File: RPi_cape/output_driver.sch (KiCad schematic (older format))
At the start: 20 parts, among them Q1 NTD5865NLT4G, U8 74LVC1G08, U9 EL3H7(TA)-VG

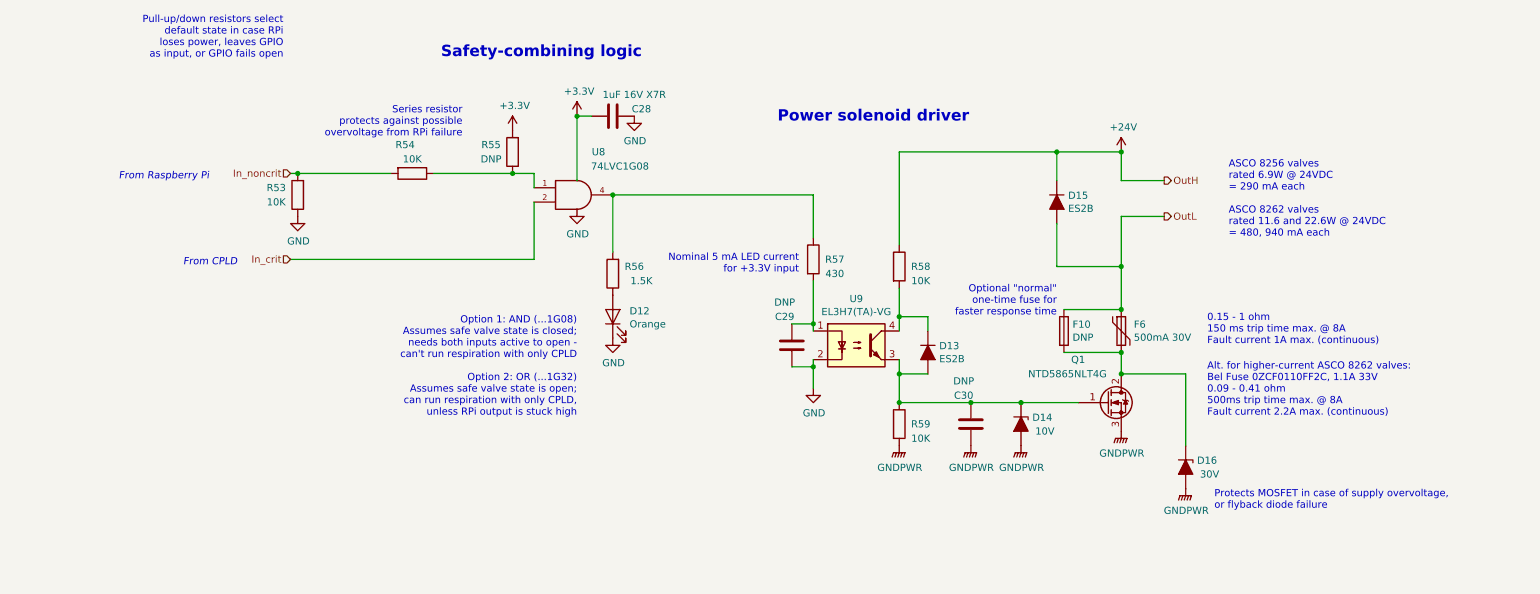
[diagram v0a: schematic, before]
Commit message: Extra info, post-design-review fixes
Added extra info on existing alternate circuit options
Added extra info on parts selection
Created initial PCB file
Added bulk cap to +5V input
Design review fixes:
Moved Raspberry Pi PWM output to GPIO18 to take advantage of hardware PWM
Fixed floating shutdown input on audio amp
Added series resistor R177 to allow low battery output to signal to both CPLD and external LED at the same time
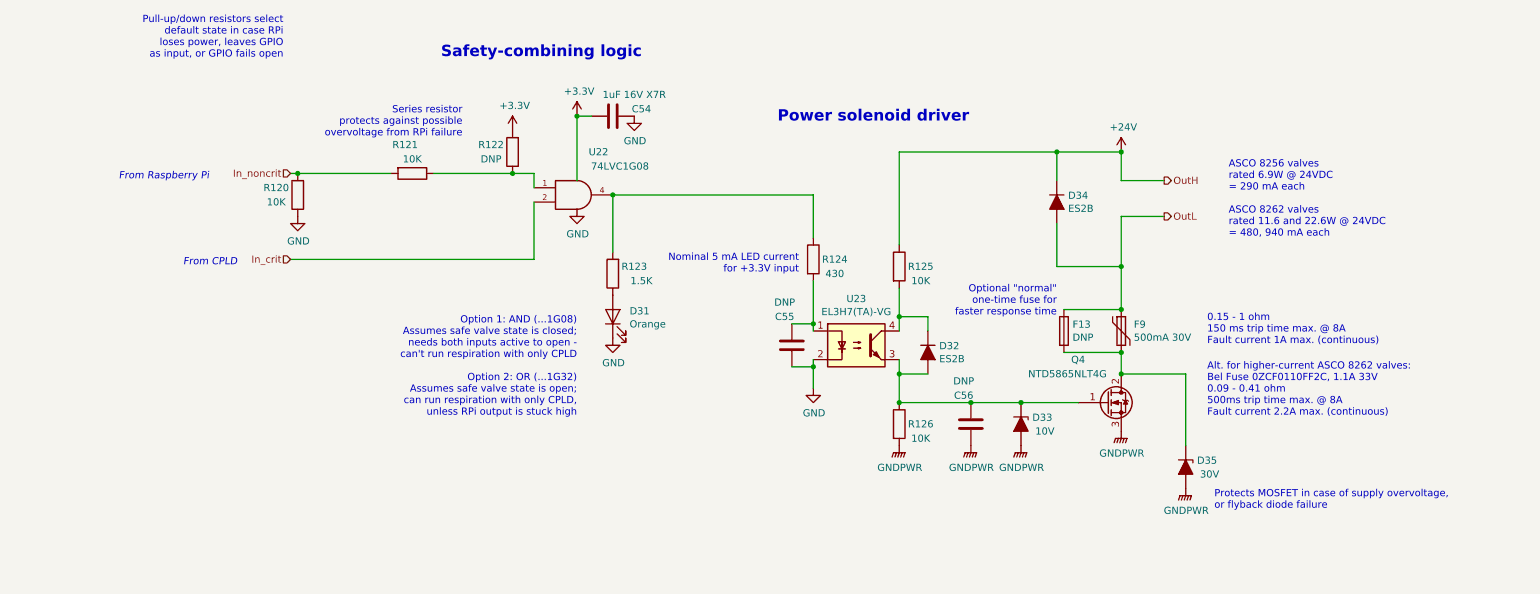
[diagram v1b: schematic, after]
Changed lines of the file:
@@
 AR Path="/5E8DFCAD/5E8FC2C2" Ref="U21"  Part="1"
 AR Path="/5E8E0754/5E8FC2C2" Ref="U23"  Part="1"
-F 0 "U9" H 6450 4025 50  0000 C CNN
+F 0 "U23" H 6450 4025 50  0000 C CNN
 F 1 "EL3H7(TA)-VG" H 6450 3934 50  0000 C CNN
 F 2 "Package_SO:SOIC-4_4.55x2.6mm_P1.27mm" H 6250 3500 50  0001 L CIN
@@
 AR Path="/5E8DFCAD/5E8FF47A" Ref="R117"  Part="1"
 AR Path="/5E8E0754/5E8FF47A" Ref="R124"  Part="1"
-F 0 "R57" H 6300 3100 50  0000 C CNN
+F 0 "R124" H 6300 3100 50  0000 C CNN
 F 1 "430" H 6300 3000 50  0000 C CNN
 F 2 "Resistor_SMD:R_1206_3216Metric" V 6080 3100 50  0001 C CNN
@@
 AR Path="/5E8DFCAD/5E900D57" Ref="#PWR0183"  Part="1"
 AR Path="/5E8E0754/5E900D57" Ref="#PWR0196"  Part="1"
-F 0 "#PWR0106" H 6150 3750 50  0001 C CNN
+F 0 "#PWR0196" H 6150 3750 50  0001 C CNN
 F 1 "GND" H 6155 3827 50  0000 C CNN
 F 2 "" H 6150 4000 50  0001 C CNN
@@
 AR Path="/5E8DFCAD/5E901311" Ref="R118"  Part="1"
 AR Path="/5E8E0754/5E901311" Ref="R125"  Part="1"
-F 0 "R58" H 6900 3150 50  0000 C CNN
+F 0 "R125" H 6900 3150 50  0000 C CNN
 F 1 "10K" H 6900 3050 50  0000 C CNN
 F 2 "Resistor_SMD:R_1206_3216Metric" V 6680 3150 50  0001 C CNN
@@
 AR Path="/5E8DFCAD/5E9015BE" Ref="R119"  Part="1"
 AR Path="/5E8E0754/5E9015BE" Ref="R126"  Part="1"
-F 0 "R59" H 6900 4250 50  0000 C CNN
+F 0 "R126" H 6900 4250 50  0000 C CNN
 F 1 "10K" H 6900 4150 50  0000 C CNN
 F 2 "Resistor_SMD:R_1206_3216Metric" V 6680 4250 50  0001 C CNN
@@
 AR Path="/5E8DFCAD/5E905A02" Ref="C53"  Part="1"
 AR Path="/5E8E0754/5E905A02" Ref="C56"  Part="1"
-F 0 "C30" H 7200 4050 50  0000 C CNN
+F 0 "C56" H 7200 4050 50  0000 C CNN
 F 1 "DNP" H 7200 3950 50  0000 C CNN
 F 2 "Capacitor_SMD:C_0805_2012Metric" H 7288 4100 50  0001 C CNN
@@
 AR Path="/5E8DFCAD/5E9088A7" Ref="D28"  Part="1"
 AR Path="/5E8E0754/5E9088A7" Ref="D33"  Part="1"
-F 0 "D14" V 7554 4329 50  0000 L CNN
+F 0 "D33" V 7554 4329 50  0000 L CNN
 F 1 "10V" V 7650 4350 50  0000 L CNN
 F 2 "Diode_SMD:D_SOD-123" H 7600 4250 50  0001 C CNN
@@
 AR Path="/5E8DFCAD/5E908F8A" Ref="Q3"  Part="1"
 AR Path="/5E8E0754/5E908F8A" Ref="Q4"  Part="1"
-F 0 "Q1" H 7950 4400 50  0000 L CNN
+F 0 "Q4" H 7950 4400 50  0000 L CNN
 F 1 "NTD5865NLT4G" H 7650 4300 50  0000 L CNN
 F 2 "Package_TO_SOT_SMD:TO-252-2" H 8400 4200 50  0001 C CNN
@@
 AR Path="/5E8DFCAD/5E909869" Ref="F8"  Part="1"
 AR Path="/5E8E0754/5E909869" Ref="F9"  Part="1"
-F 0 "F6" H 8388 3646 50  0000 L CNN
+F 0 "F9" H 8388 3646 50  0000 L CNN
 F 1 "500mA 30V" H 8388 3555 50  0000 L CNN
 F 2 "Fuse:Fuse_2920_7451Metric" H 8350 3400 50  0001 L CNN
@@
 AR Path="/5E8DFCAD/5E90C94B" Ref="D30"  Part="1"
 AR Path="/5E8E0754/5E90C94B" Ref="D35"  Part="1"
-F 0 "D16" V 8704 4629 50  0000 L CNN
+F 0 "D35" V 8704 4629 50  0000 L CNN
 F 1 "30V" V 8800 4650 50  0000 L CNN
 F 2 "Diode_SMD:D_SMA" H 8750 4550 50  0001 C CNN
@@
 AR Path="/5E8DFCAD/5E90D582" Ref="D29"  Part="1"
 AR Path="/5E8E0754/5E90D582" Ref="D34"  Part="1"
-F 0 "D15" V 7804 2779 50  0000 L CNN
+F 0 "D34" V 7804 2779 50  0000 L CNN
 F 1 "ES2B" V 7895 2779 50  0000 L CNN
 F 2 "Diode_SMD:D_SMA" H 7850 2700 50  0001 C CNN
@@
 AR Path="/5E8DFCAD/5E913275" Ref="D27"  Part="1"
 AR Path="/5E8E0754/5E913275" Ref="D32"  Part="1"
-F 0 "D13" V 6904 3829 50  0000 L CNN
+F 0 "D32" V 6904 3829 50  0000 L CNN
 F 1 "ES2B" V 6995 3829 50  0000 L CNN
 F 2 "Diode_SMD:D_SMA" H 6950 3750 50  0001 C CNN
@@
 AR Path="/5E8DFCAD/5E880DD0" Ref="#PWR0189"  Part="1"
 AR Path="/5E8E0754/5E880DD0" Ref="#PWR0202"  Part="1"
-F 0 "#PWR0112" H 8750 4500 50  0001 C CNN
+F 0 "#PWR0202" H 8750 4500 50  0001 C CNN
 F 1 "GNDPWR" H 8754 4546 50  0000 C CNN
 F 2 "" H 8750 4650 50  0001 C CNN
@@
 AR Path="/5E8DFCAD/5E8842DE" Ref="#PWR0187"  Part="1"
 AR Path="/5E8E0754/5E8842DE" Ref="#PWR0200"  Part="1"
-F 0 "#PWR0110" H 8300 2200 50  0001 C CNN
+F 0 "#PWR0200" H 8300 2200 50  0001 C CNN
 F 1 "+24V" H 8315 2523 50  0000 C CNN
 F 2 "" H 8300 2350 50  0001 C CNN
@@
 AR Path="/5E8DFCAD/5E88C1E4" Ref="C52"  Part="1"
 AR Path="/5E8E0754/5E88C1E4" Ref="C55"  Part="1"
-F 0 "C29" H 5950 3500 50  0000 C CNN
+F 0 "C55" H 5950 3500 50  0000 C CNN
 F 1 "DNP" H 5950 3400 50  0000 C CNN
 F 2 "Capacitor_SMD:C_0805_2012Metric" H 6038 3550 50  0001 C CNN
@@
 AR Path="/5E8DFCAD/5EA15643" Ref="U20"  Part="1"
 AR Path="/5E8DEDC0/5EA15643" Ref="U18"  Part="1"
-F 0 "U8" H 4650 2950 50  0000 C CNN
+F 0 "U22" H 4650 2950 50  0000 C CNN
 F 1 "74LVC1G08" H 4800 2850 50  0000 C CNN
 F 2 "Package_TO_SOT_SMD:SOT-23-5" H 4500 2650 50  0001 C CNN
@@
 AR Path="/5E8DFCAD/5EA17709" Ref="#PWR0180"  Part="1"
 AR Path="/5E8E0754/5EA17709" Ref="#PWR0193"  Part="1"
-F 0 "#PWR0103" H 4500 2500 50  0001 C CNN
+F 0 "#PWR0193" H 4500 2500 50  0001 C CNN
 F 1 "GND" H 4505 2577 50  0000 C CNN
 F 2 "" H 4500 2750 50  0001 C CNN
@@
 AR Path="/5E8DFCAD/5EA197B0" Ref="#PWR0179"  Part="1"
 AR Path="/5E8DEDC0/5EA197B0" Ref="#PWR0166"  Part="1"
-F 0 "#PWR0102" H 4500 1950 50  0001 C CNN
+F 0 "#PWR0192" H 4500 1950 50  0001 C CNN
 F 1 "+3.3V" H 4515 2273 50  0000 C CNN
 F 2 "" H 4500 2100 50  0001 C CNN
@@
 AR Path="/5E8DFCAD/5EA25A46" Ref="#PWR0182"  Part="1"
 AR Path="/5E8DEDC0/5EA25A46" Ref="#PWR0169"  Part="1"
-F 0 "#PWR0105" H 4900 1850 50  0001 C CNN
+F 0 "#PWR0195" H 4900 1850 50  0001 C CNN
 F 1 "GND" H 4905 1927 50  0000 C CNN
 F 2 "" H 4900 2100 50  0001 C CNN
@@
 AR Path="/5E8DFCAD/5EA25A4C" Ref="C51"  Part="1"
 AR Path="/5E8DEDC0/5EA25A4C" Ref="C48"  Part="1"
-F 0 "C28" V 4700 2300 50  0000 C CNN
+F 0 "C54" V 4700 2300 50  0000 C CNN
 F 1 "1uF 16V X7R" V 4600 2250 50  0000 C CNN
 F 2 "Capacitor_SMD:C_0805_2012Metric" H 4788 1950 50  0001 C CNN
@@
 AR Path="/5E8DFCAD/5EAB3FCE" Ref="R113"  Part="1"
 AR Path="/5E8E0754/5EAB3FCE" Ref="R120"  Part="1"
-F 0 "R53" H 2700 2600 50  0000 C CNN
+F 0 "R120" H 2700 2600 50  0000 C CNN
 F 1 "10K" H 2700 2700 50  0000 C CNN
 F 2 "Resistor_SMD:R_1206_3216Metric" V 2480 2650 50  0001 C CNN
@@
 AR Path="/5E8DFCAD/5EAB68F6" Ref="#PWR0177"  Part="1"
 AR Path="/5E8E0754/5EAB68F6" Ref="#PWR0190"  Part="1"
-F 0 "#PWR0100" H 2550 2550 50  0001 C CNN
+F 0 "#PWR0190" H 2550 2550 50  0001 C CNN
 F 1 "GND" H 2555 2627 50  0000 C CNN
 F 2 "" H 2550 2800 50  0001 C CNN
@@
 AR Path="/5E8DFCAD/5EB47B74" Ref="R115"  Part="1"
 AR Path="/5E8E0754/5EB47B74" Ref="R122"  Part="1"
-F 0 "R55" H 4200 2300 50  0000 C CNN
+F 0 "R122" H 4200 2300 50  0000 C CNN
 F 1 "DNP" H 4200 2400 50  0000 C CNN
 F 2 "Resistor_SMD:R_1206_3216Metric" V 3980 2350 50  0001 C CNN
@@
 AR Path="/5E8DFCAD/5EB49CAF" Ref="#PWR0178"  Part="1"
 AR Path="/5E8DEDC0/5EB49CAF" Ref="#PWR0165"  Part="1"
-F 0 "#PWR0101" H 4050 2050 50  0001 C CNN
+F 0 "#PWR0191" H 4050 2050 50  0001 C CNN
 F 1 "+3.3V" H 4065 2373 50  0000 C CNN
 F 2 "" H 4050 2200 50  0001 C CNN
@@
 AR Path="/5E8DFCAD/5EA292AA" Ref="R114"  Part="1"
 AR Path="/5E8E0754/5EA292AA" Ref="R121"  Part="1"
-F 0 "R54" V 3150 2450 50  0000 C CNN
+F 0 "R121" V 3150 2450 50  0000 C CNN
 F 1 "10K" V 3250 2500 50  0000 C CNN
 F 2 "Resistor_SMD:R_1206_3216Metric" V 3280 2500 50  0001 C CNN
@@
 AR Path="/5E8DFCAD/5F8B2D08" Ref="D26"  Part="1"
 AR Path="/5E8E0754/5F8B2D08" Ref="D31"  Part="1"
-F 0 "D12" V 4789 3383 50  0000 R CNN
+F 0 "D31" V 4789 3383 50  0000 R CNN
 F 1 "Orange" V 4698 3383 50  0000 R CNN
 F 2 "LED_SMD:LED_0805_2012Metric" H 4750 3500 50  0001 C CNN
@@
 AR Path="/5E8DEDC0/5F8B2D0E" Ref="#PWR0168"  Part="1"
 AR Path="/5E8C8865/5F8B2D0E" Ref="#PWR?"  Part="1"
-F 0 "#PWR0104" H 4750 3400 50  0001 C CNN
+F 0 "#PWR0194" H 4750 3400 50  0001 C CNN
 F 1 "GND" H 4755 3477 50  0000 C CNN
 F 2 "" H 4750 3650 50  0001 C CNN
@@
 AR Path="/5E8DFCAD/5F8B2D14" Ref="R116"  Part="1"
 AR Path="/5E8E0754/5F8B2D14" Ref="R123"  Part="1"
-F 0 "R56" H 4600 3150 50  0000 C CNN
+F 0 "R123" H 4600 3150 50  0000 C CNN
 F 1 "1.5K" H 4550 3250 50  0000 C CNN
 F 2 "Resistor_SMD:R_1206_3216Metric" V 4680 3200 50  0001 C CNN
@@
 AR Path="/5E8DFCAD/5FA3BD23" Ref="F12"  Part="1"
 AR Path="/5E8E0754/5FA3BD23" Ref="F13"  Part="1"
-F 0 "F10" H 7960 3646 50  0000 L CNN
+F 0 "F13" H 7960 3646 50  0000 L CNN
 F 1 "DNP" H 7960 3555 50  0000 L CNN
 F 2 "Fuse:Fuse_1206_3216Metric" V 7830 3600 50  0001 C CNN
@@
 AR Path="/5E8DFCAD/5E882AC5" Ref="#PWR0184"  Part="1"
 AR Path="/5E8E0754/5E882AC5" Ref="#PWR0197"  Part="1"
-F 0 "#PWR0107" H 6750 4200 50  0001 C CNN
+F 0 "#PWR0197" H 6750 4200 50  0001 C CNN
 F 1 "GNDPWR" H 6754 4246 50  0000 C CNN
 F 2 "" H 6750 4350 50  0001 C CNN
@@
 AR Path="/5E8DFCAD/5E88277D" Ref="#PWR0185"  Part="1"
 AR Path="/5E8E0754/5E88277D" Ref="#PWR0198"  Part="1"
-F 0 "#PWR0108" H 7250 4200 50  0001 C CNN
+F 0 "#PWR0198" H 7250 4200 50  0001 C CNN
 F 1 "GNDPWR" H 7254 4246 50  0000 C CNN
 F 2 "" H 7250 4350 50  0001 C CNN
@@
 AR Path="/5E8DFCAD/5E882430" Ref="#PWR0186"  Part="1"
 AR Path="/5E8E0754/5E882430" Ref="#PWR0199"  Part="1"
-F 0 "#PWR0109" H 7600 4200 50  0001 C CNN
+F 0 "#PWR0199" H 7600 4200 50  0001 C CNN
 F 1 "GNDPWR" H 7604 4246 50  0000 C CNN
 F 2 "" H 7600 4350 50  0001 C CNN
@@
 AR Path="/5E8DFCAD/5E881F2F" Ref="#PWR0188"  Part="1"
 AR Path="/5E8E0754/5E881F2F" Ref="#PWR0201"  Part="1"
-F 0 "#PWR0111" H 8300 4100 50  0001 C CNN
+F 0 "#PWR0201" H 8300 4100 50  0001 C CNN
 F 1 "GNDPWR" H 8304 4146 50  0000 C CNN
 F 2 "" H 8300 4250 50  0001 C CNN

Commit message: Finished layout, minor design changes
Assigned CPLD pins
Finished routing PCB
Moved rotary encoder inputs to CPLD
Removed separate decoupling caps for smaller CPLD footprint due to routing constraints
Added pull-downs on CPLD inputs for each valve driver (R198 etc.)
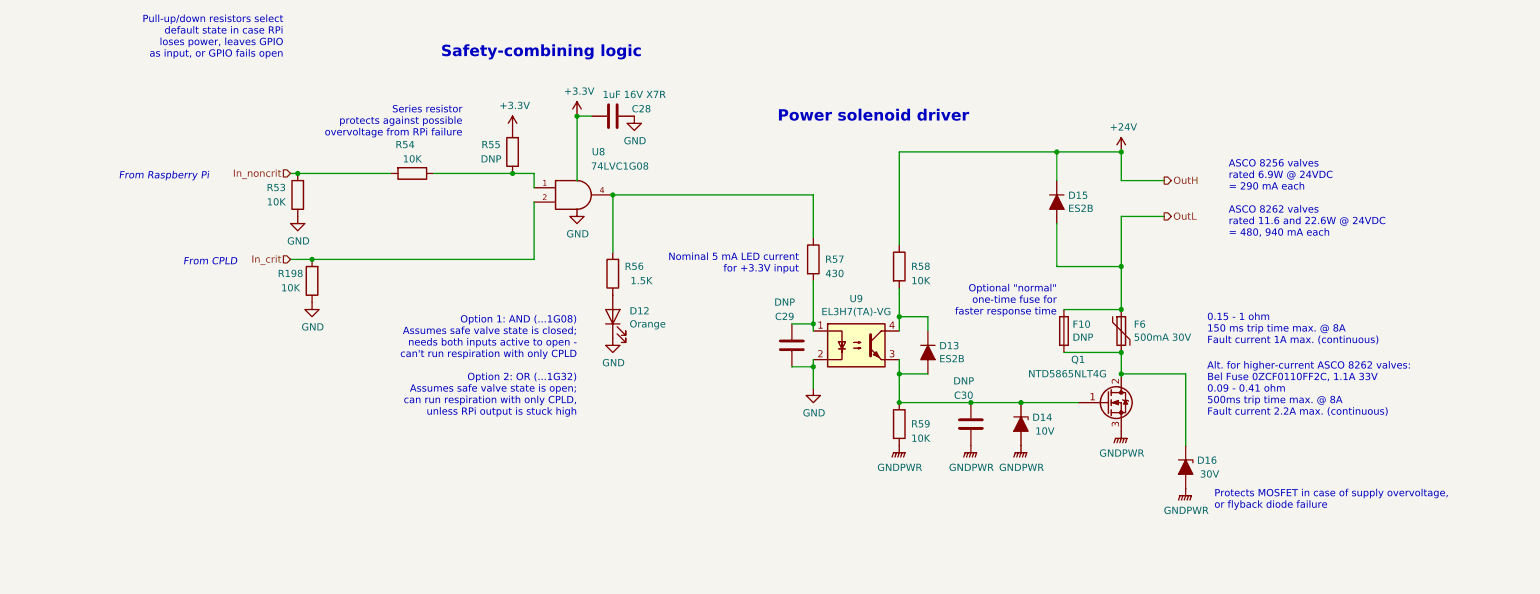
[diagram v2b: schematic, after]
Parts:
- added R198: 10K, Resistor_SMD:R_1206_3216Metric, symbol Device:R
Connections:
- net GND: now also R198.1
- net In_crit: now also R198.2
